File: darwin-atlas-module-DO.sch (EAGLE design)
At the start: 24 parts, among them J1 2X6-HEADERS, U3 M24C02-WMN6TP

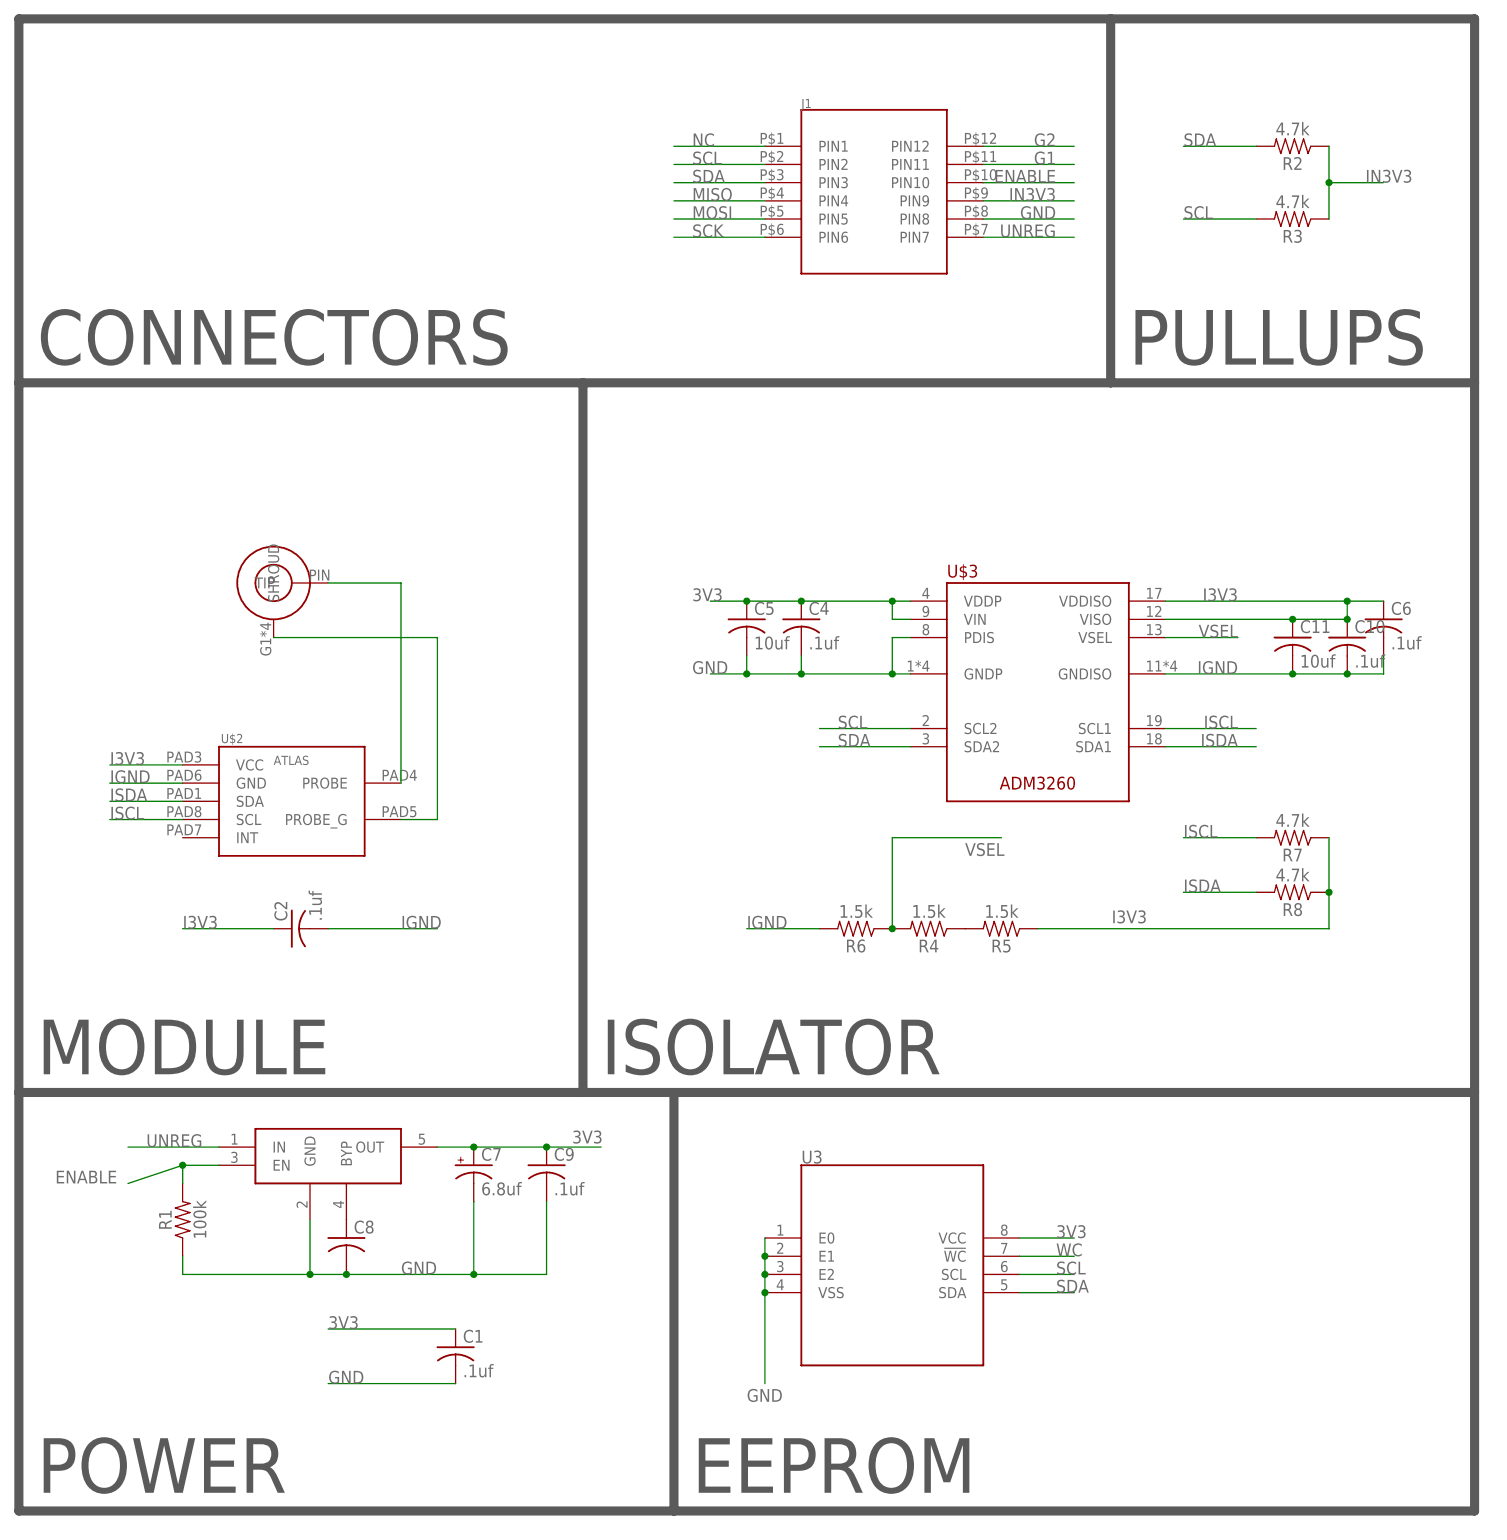
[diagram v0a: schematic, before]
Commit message: Forked D.O. Variant and added barometric pressure sensor to it.
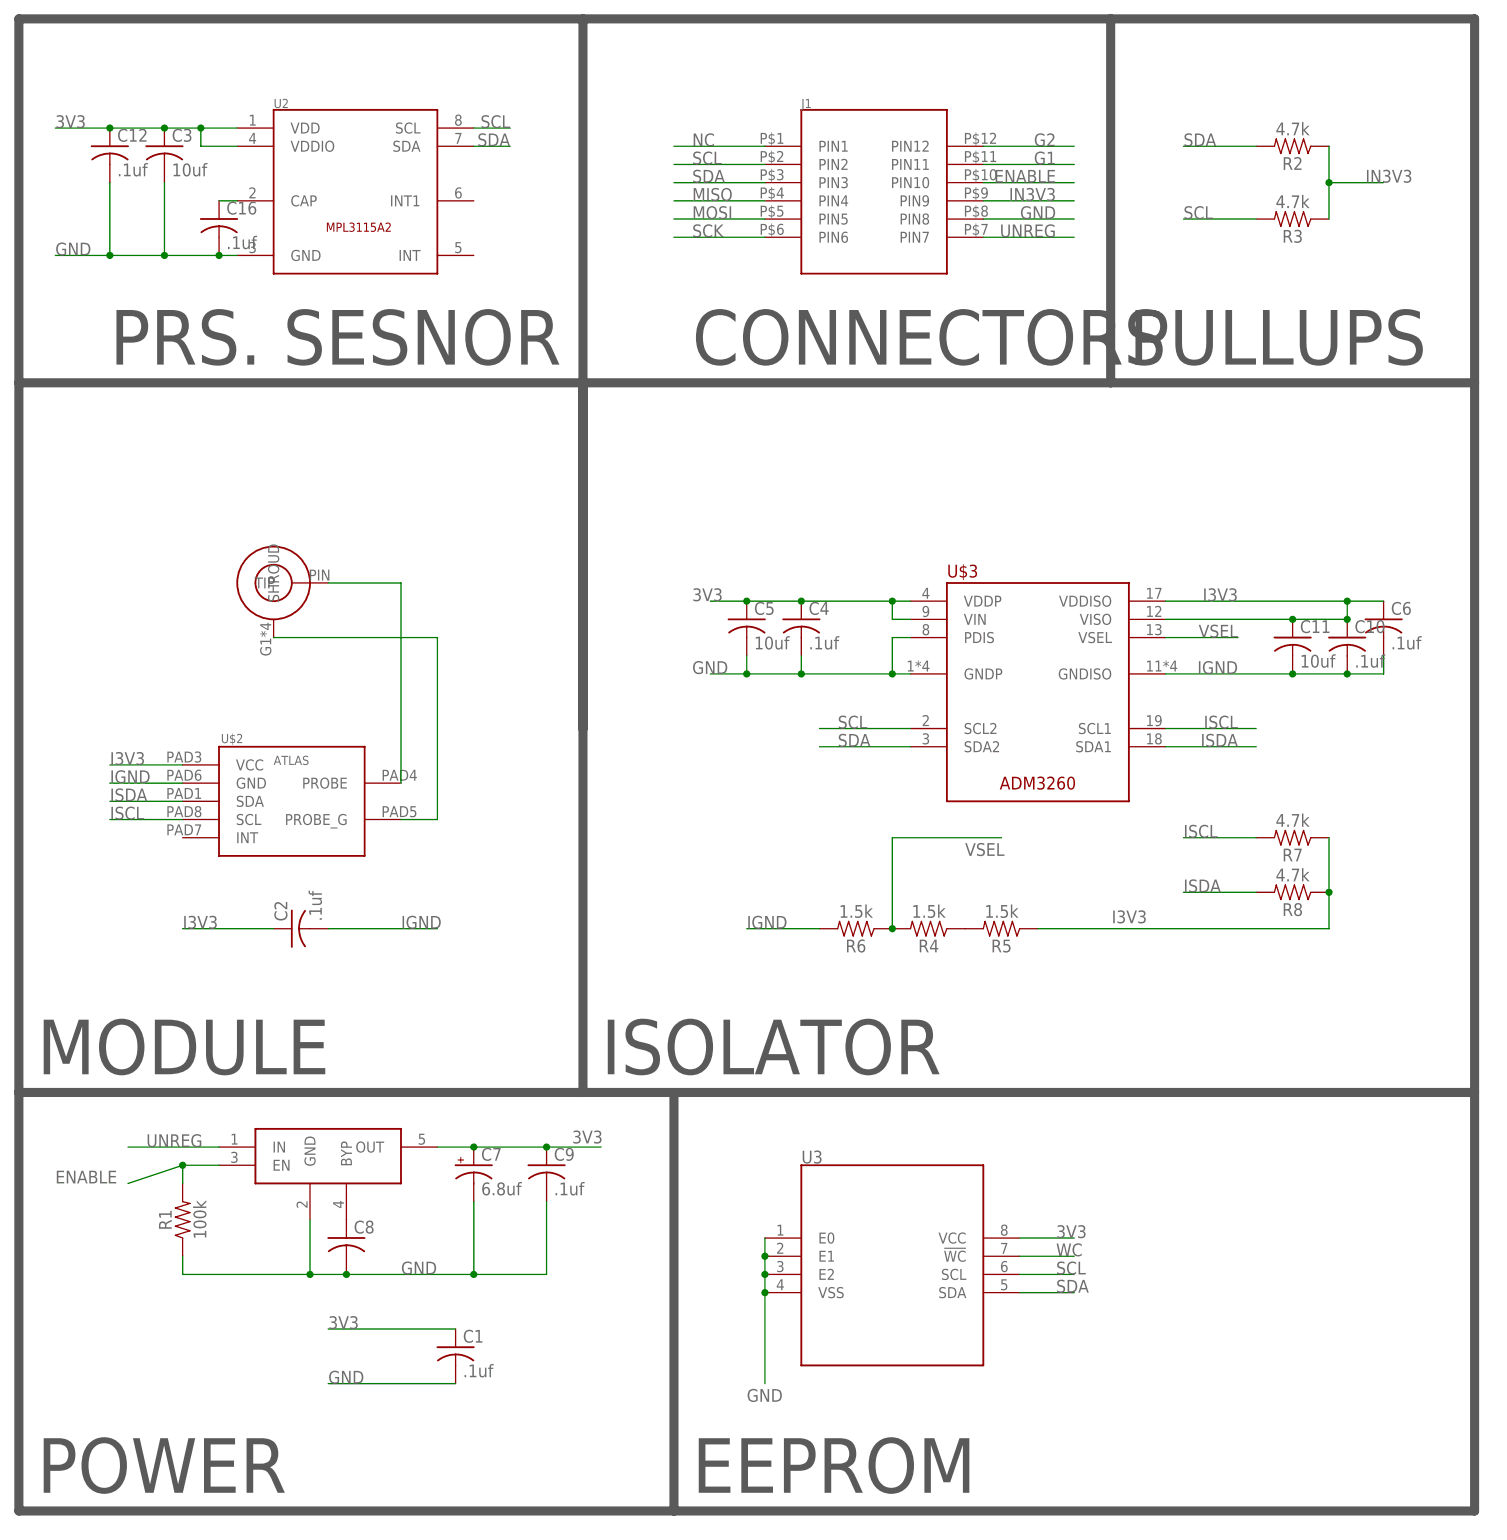
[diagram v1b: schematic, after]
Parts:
- added C12, C16: .1uf, rcl:C-USC0603K
- added C3: 10uf, rcl:C-USC0603K
- added U2: MPL3115A2LGA8, Conservify:MPL3115A2LGA8
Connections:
- new net CAP: C16.1, U2.CAP
- net 3V3: now also C12.1, C3.1, U2.VDD, U2.VDDIO
- net GND: now also C12.2, C16.2, C3.2, U2.GND
- net SCL: now also U2.SCL
- net SDA: now also U2.SDA
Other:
- note added: "PRS. SESNOR"
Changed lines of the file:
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@@
 <part name="R7" library="SparkFun-Resistors" library_urn="urn:adsk.eagle:library:532" deviceset="100KOHM" device="-0603-1/10W-1%" package3d_urn="urn:adsk.eagle:package:39650/1" value="4.7k"/>
 <part name="R8" library="SparkFun-Resistors" library_urn="urn:adsk.eagle:library:532" deviceset="100KOHM" device="-0603-1/10W-1%" package3d_urn="urn:adsk.eagle:package:39650/1" value="4.7k"/>
+<part name="U2" library="Conservify" library_urn="urn:adsk.eagle:library:11839183" deviceset="MPL3115A2" device="LGA8" package3d_urn="urn:adsk.eagle:package:11890235/2"/>
+<part name="C3" library="rcl" library_urn="urn:adsk.eagle:library:334" deviceset="C-US" device="C0603K" package3d_urn="urn:adsk.eagle:package:23680/2" value="10uf"/>
+<part name="C12" library="rcl" library_urn="urn:adsk.eagle:library:334" deviceset="C-US" device="C0603K" package3d_urn="urn:adsk.eagle:package:23680/2" value=".1uf"/>
+<part name="C16" library="rcl" library_urn="urn:adsk.eagle:library:334" deviceset="C-US" device="C0603K" package3d_urn="urn:adsk.eagle:package:23680/2" value=".1uf"/>
 </parts>
 <sheets>
 <sheet>
 <plain>
-<text x="43.18" y="66.04" size="7.62" layer="97">CONNECTORS</text>
+<text x="134.62" y="66.04" size="7.62" layer="97">CONNECTORS</text>
 <text x="43.18" y="-91.44" size="7.62" layer="97">POWER</text>
 <text x="134.62" y="-91.44" size="7.62" layer="97">EEPROM</text>
-<wire x1="40.64" y1="114.3" x2="193.04" y2="114.3" width="1.27" layer="97"/>
+<wire x1="40.64" y1="114.3" x2="119.38" y2="114.3" width="1.27" layer="97"/>
+<wire x1="119.38" y1="114.3" x2="193.04" y2="114.3" width="1.27" layer="97"/>
 <wire x1="193.04" y1="114.3" x2="193.04" y2="63.5" width="1.27" layer="97"/>
 <wire x1="193.04" y1="63.5" x2="119.38" y2="63.5" width="1.27" layer="97"/>
@@
 <wire x1="40.64" y1="63.5" x2="40.64" y2="-35.56" width="1.27" layer="97"/>
 <wire x1="40.64" y1="-35.56" x2="119.38" y2="-35.56" width="1.27" layer="97"/>
-<wire x1="119.38" y1="-35.56" x2="119.38" y2="63.5" width="1.27" layer="97"/>
+<wire x1="119.38" y1="-35.56" x2="119.38" y2="15.24" width="1.27" layer="97"/>
+<wire x1="119.38" y1="15.24" x2="119.38" y2="63.5" width="1.27" layer="97"/>
 <wire x1="119.38" y1="-35.56" x2="132.08" y2="-35.56" width="1.27" layer="97"/>
 <wire x1="132.08" y1="-35.56" x2="243.84" y2="-35.56" width="1.27" layer="97"/>
@@
 <text x="121.92" y="-33.02" size="7.62" layer="97">ISOLATOR</text>
 <wire x1="243.84" y1="63.5" x2="243.84" y2="-35.56" width="1.27" layer="97"/>
+<wire x1="119.38" y1="15.24" x2="119.38" y2="114.3" width="1.27" layer="97"/>
+<text x="53.34" y="66.04" size="7.62" layer="97">PRS. SESNOR</text>
 </plain>
 <instances>
@@
 <attribute name="NAME" x="218.44" y="-9.144" size="1.778" layer="95" font="vector" rot="R180" align="bottom-center"/>
 <attribute name="VALUE" x="218.44" y="-6.096" size="1.778" layer="96" font="vector" rot="R180" align="top-center"/>
+</instance>
+<instance part="U2" gate="G$1" x="88.9" y="91.44" smashed="yes">
+<attribute name="NAME" x="76.2" y="101.854" size="1.27" layer="95"/>
+</instance>
+<instance part="C3" gate="G$1" x="60.96" y="96.52" smashed="yes">
+<attribute name="NAME" x="61.976" y="97.155" size="1.778" layer="95"/>
+<attribute name="VALUE" x="61.976" y="92.329" size="1.778" layer="96"/>
+</instance>
+<instance part="C12" gate="G$1" x="53.34" y="96.52" smashed="yes">
+<attribute name="NAME" x="54.356" y="97.155" size="1.778" layer="95"/>
+<attribute name="VALUE" x="54.356" y="92.329" size="1.778" layer="96"/>
+</instance>
+<instance part="C16" gate="G$1" x="68.58" y="86.36" smashed="yes">
+<attribute name="NAME" x="69.596" y="86.995" size="1.778" layer="95"/>
+<attribute name="VALUE" x="69.596" y="82.169" size="1.778" layer="96"/>
 </instance>
 </instances>
@@
 <junction x="149.86" y="22.86"/>
 </segment>
+<segment>
+<pinref part="U2" gate="G$1" pin="GND"/>
+<wire x1="71.12" y1="81.28" x2="68.58" y2="81.28" width="0.1524" layer="91"/>
+<label x="45.72" y="81.28" size="1.778" layer="95"/>
+<pinref part="C16" gate="G$1" pin="2"/>
+<wire x1="68.58" y1="81.28" x2="60.96" y2="81.28" width="0.1524" layer="91"/>
+<junction x="68.58" y="81.28"/>
+<pinref part="C12" gate="G$1" pin="2"/>
+<wire x1="60.96" y1="81.28" x2="53.34" y2="81.28" width="0.1524" layer="91"/>
+<wire x1="53.34" y1="91.44" x2="53.34" y2="81.28" width="0.1524" layer="91"/>
+<junction x="53.34" y="81.28"/>
+<pinref part="C3" gate="G$1" pin="2"/>
+<wire x1="60.96" y1="91.44" x2="60.96" y2="81.28" width="0.1524" layer="91"/>
+<junction x="60.96" y="81.28"/>
+<wire x1="53.34" y1="81.28" x2="45.72" y2="81.28" width="0.1524" layer="91"/>
+</segment>
 </net>
 <net name="3V3" class="0">
@@
 <junction x="142.24" y="33.02"/>
 </segment>
+<segment>
+<pinref part="U2" gate="G$1" pin="VDD"/>
+<wire x1="71.12" y1="99.06" x2="66.04" y2="99.06" width="0.1524" layer="91"/>
+<label x="45.72" y="99.06" size="1.778" layer="95"/>
+<pinref part="C3" gate="G$1" pin="1"/>
+<pinref part="C12" gate="G$1" pin="1"/>
+<wire x1="66.04" y1="99.06" x2="60.96" y2="99.06" width="0.1524" layer="91"/>
+<wire x1="60.96" y1="99.06" x2="53.34" y2="99.06" width="0.1524" layer="91"/>
+<junction x="60.96" y="99.06"/>
+<wire x1="53.34" y1="99.06" x2="45.72" y2="99.06" width="0.1524" layer="91"/>
+<junction x="53.34" y="99.06"/>
+<pinref part="U2" gate="G$1" pin="VDDIO"/>
+<wire x1="71.12" y1="96.52" x2="66.04" y2="96.52" width="0.1524" layer="91"/>
+<wire x1="66.04" y1="96.52" x2="66.04" y2="99.06" width="0.1524" layer="91"/>
+<junction x="66.04" y="99.06"/>
+</segment>
 </net>
 <net name="N$6" class="0">
@@
 <label x="154.94" y="12.7" size="1.778" layer="95"/>
 </segment>
+<segment>
+<pinref part="U2" gate="G$1" pin="SDA"/>
+<wire x1="104.14" y1="96.52" x2="109.22" y2="96.52" width="0.1524" layer="91"/>
+<label x="109.22" y="96.52" size="1.778" layer="95" align="bottom-right"/>
+</segment>
 </net>
 <net name="SCL" class="0">
@@
 <wire x1="165.1" y1="15.24" x2="152.4" y2="15.24" width="0.1524" layer="91"/>
 <label x="154.94" y="15.24" size="1.778" layer="95"/>
+</segment>
+<segment>
+<pinref part="U2" gate="G$1" pin="SCL"/>
+<wire x1="104.14" y1="99.06" x2="109.22" y2="99.06" width="0.1524" layer="91"/>
+<label x="109.22" y="99.06" size="1.778" layer="95" align="bottom-right"/>
 </segment>
 </net>
@@
 </segment>
 </net>
+<net name="CAP" class="0">
+<segment>
+<pinref part="U2" gate="G$1" pin="CAP"/>
+<wire x1="71.12" y1="88.9" x2="68.58" y2="88.9" width="0.1524" layer="91"/>
+<pinref part="C16" gate="G$1" pin="1"/>
+</segment>
+</net>
